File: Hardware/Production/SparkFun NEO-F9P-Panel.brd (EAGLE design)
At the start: 160.8 x 107.4 mm, 822 parts, among them J1 ANTENNA-SMA-GROUNDEDEDGE_SMA, J11 ANTENNA-SMA-GROUNDEDEDGE_SMA, J15 Qwiic Right Angle, J16 Qwiic Right Angle, J18 ANTENNA-SMA-GROUNDEDEDGE_SMA, J2 Qwiic Right Angle, J22 Qwiic Right Angle, J23 Qwiic Right Angle, J25 ANTENNA-SMA-GROUNDEDEDGE_SMA, J29 Qwiic Right Angle, J30 Qwiic Right Angle, J32 ANTENNA-SMA-GROUNDEDEDGE_SMA, J36 Qwiic Right Angle, J37 Qwiic Right Angle, J39 ANTENNA-SMA-GROUNDEDEDGE_SMA, J4 Qwiic Right Angle, J8 Qwiic Right Angle, J9 Qwiic Right Angle, U1 U-BLOX_NEO-F9P-15B, U10 U-BLOX_NEO-F9P-15B, U11 3.3V, U12 U-BLOX_NEO-F9P-15B, U2 3.3V, U3 3.3V, U4 U-BLOX_NEO-F9P-15B, U5 3.3V, U6 U-BLOX_NEO-F9P-15B, U7 3.3V, U8 U-BLOX_NEO-F9P-15B, U9 3.3V

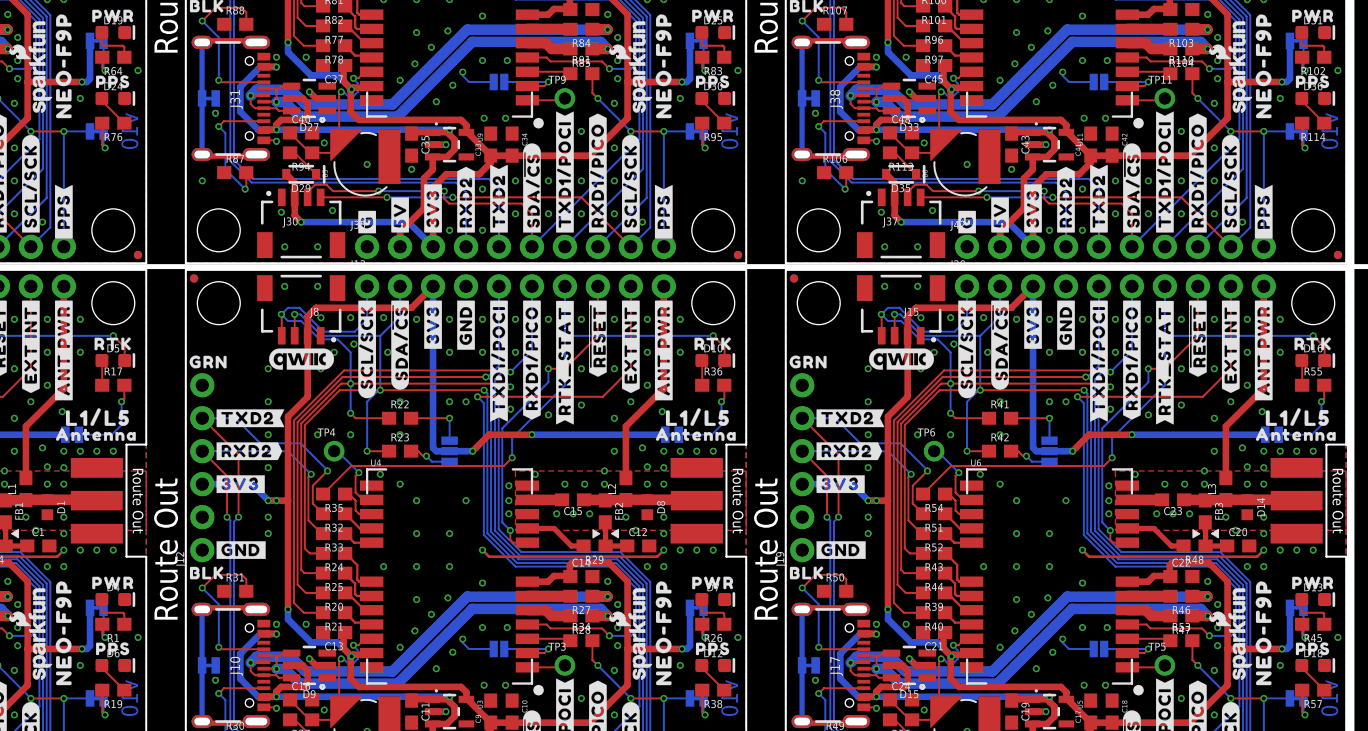
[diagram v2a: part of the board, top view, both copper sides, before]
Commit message: Adjust layout post design review.
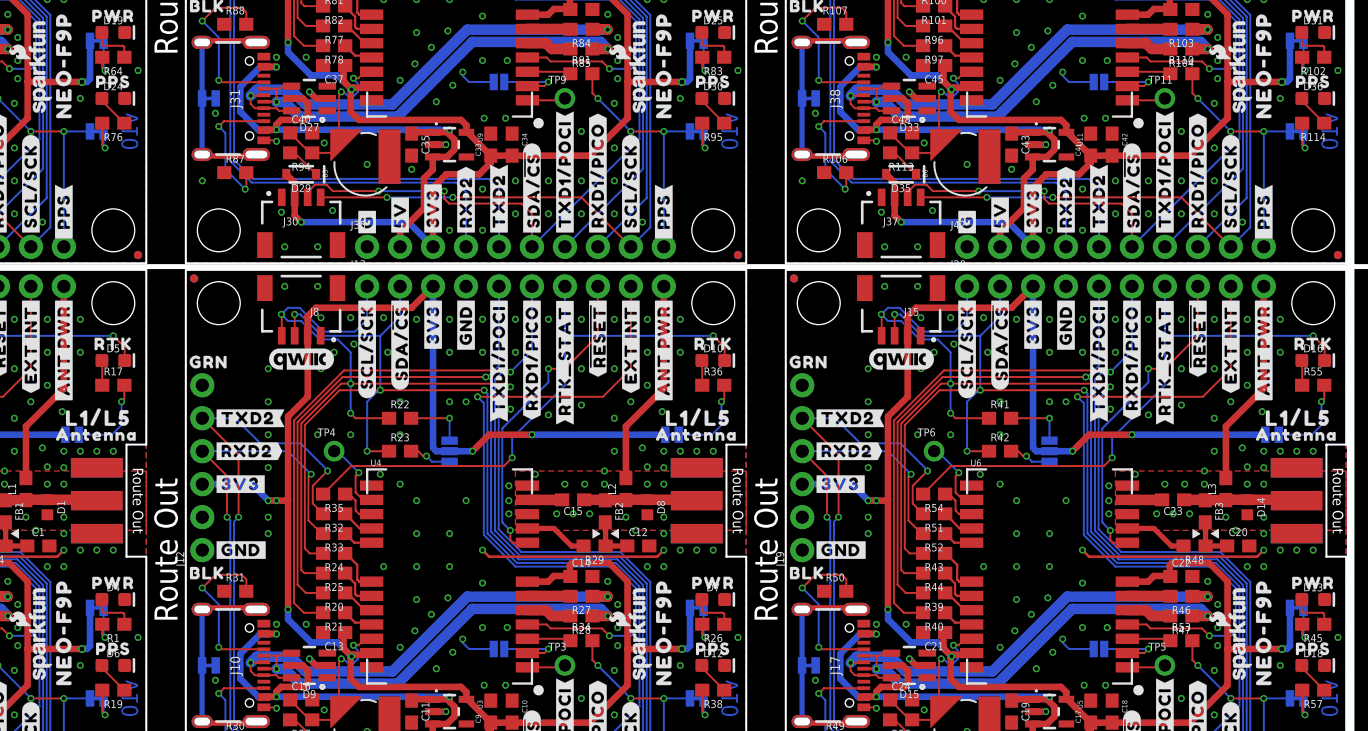
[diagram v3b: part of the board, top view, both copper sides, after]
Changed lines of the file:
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@@
 <wire x1="9.39" y1="38.1" x2="9.39" y2="33.3951875" width="0.508" layer="1"/>
 <wire x1="38.8493" y1="17.145" x2="38.8493" y2="14.2113" width="0.508" layer="16"/>
-<wire x1="38.8493" y1="14.2113" x2="38.608" y2="13.97" width="0.508" layer="16"/>
-<wire x1="38.608" y1="13.97" x2="38.227" y2="13.97" width="0.508" layer="16"/>
-<via x="38.227" y="13.97" extent="1-16" drill="0.3048"/>
 <wire x1="38.226996875" y1="13.97" x2="34.036" y2="13.97" width="0.508" layer="1"/>
 <contactref element="J6" pad="3"/>
@@
 <wire x1="22.098" y1="29.21" x2="20.32" y2="29.21" width="0.508" layer="16"/>
 <wire x1="36.9443" y1="30.48" x2="26.67" y2="30.48" width="0.508" layer="16"/>
-<wire x1="38.226996875" y1="13.97" x2="38.227" y2="13.97" width="0" layer="19" extent="1-1"/>
+<wire x1="38.8493" y1="14.2113" x2="38.608" y2="13.97" width="0.508" layer="16"/>
+<wire x1="38.608" y1="13.97" x2="38.226996875" y2="13.97" width="0.508" layer="16"/>
+<via x="38.226996875" y="13.97" extent="1-16" drill="0.381"/>
 </signal>
 <signal name="GND">
@@
 <wire x1="55.618" y1="38.1" x2="55.618" y2="33.3951875" width="0.508" layer="1"/>
 <wire x1="85.0773" y1="17.145" x2="85.0773" y2="14.2113" width="0.508" layer="16"/>
-<wire x1="85.0773" y1="14.2113" x2="84.836" y2="13.97" width="0.508" layer="16"/>
-<wire x1="84.836" y1="13.97" x2="84.455" y2="13.97" width="0.508" layer="16"/>
-<via x="84.455" y="13.97" extent="1-16" drill="0.3048"/>
 <wire x1="84.454996875" y1="13.97" x2="80.264" y2="13.97" width="0.508" layer="1"/>
 <contactref element="J14" pad="3"/>
@@
 <wire x1="68.326" y1="29.21" x2="66.548" y2="29.21" width="0.508" layer="16"/>
 <wire x1="83.1723" y1="30.48" x2="72.898" y2="30.48" width="0.508" layer="16"/>
-<wire x1="84.454996875" y1="13.97" x2="84.455" y2="13.97" width="0" layer="19" extent="1-1"/>
+<wire x1="85.0773" y1="14.2113" x2="84.836" y2="13.97" width="0.508" layer="16"/>
+<wire x1="84.836" y1="13.97" x2="84.454996875" y2="13.97" width="0.508" layer="16"/>
+<via x="84.454996875" y="13.97" extent="1-16" drill="0.381"/>
 </signal>
 <signal name="GND1">
@@
 <wire x1="101.846" y1="38.1" x2="101.846" y2="33.3951875" width="0.508" layer="1"/>
 <wire x1="131.3053" y1="17.145" x2="131.3053" y2="14.2113" width="0.508" layer="16"/>
-<wire x1="131.3053" y1="14.2113" x2="131.064" y2="13.97" width="0.508" layer="16"/>
-<wire x1="131.064" y1="13.97" x2="130.683" y2="13.97" width="0.508" layer="16"/>
-<via x="130.683" y="13.97" extent="1-16" drill="0.3048"/>
 <wire x1="130.682996875" y1="13.97" x2="126.492" y2="13.97" width="0.508" layer="1"/>
 <contactref element="J21" pad="3"/>
@@
 <wire x1="114.554" y1="29.21" x2="112.776" y2="29.21" width="0.508" layer="16"/>
 <wire x1="129.4003" y1="30.48" x2="119.126" y2="30.48" width="0.508" layer="16"/>
-<wire x1="130.682996875" y1="13.97" x2="130.683" y2="13.97" width="0" layer="19" extent="1-1"/>
+<wire x1="131.3053" y1="14.2113" x2="131.064" y2="13.97" width="0.508" layer="16"/>
+<wire x1="131.064" y1="13.97" x2="130.682996875" y2="13.97" width="0.508" layer="16"/>
+<via x="130.682996875" y="13.97" extent="1-16" drill="0.381"/>
 </signal>
 <signal name="GND2">
@@
 <wire x1="9.39" y1="81.788" x2="9.39" y2="77.0831875" width="0.508" layer="1"/>
 <wire x1="38.8493" y1="60.833" x2="38.8493" y2="57.8993" width="0.508" layer="16"/>
-<wire x1="38.8493" y1="57.8993" x2="38.608" y2="57.658" width="0.508" layer="16"/>
-<wire x1="38.608" y1="57.658" x2="38.227" y2="57.658" width="0.508" layer="16"/>
-<via x="38.227" y="57.658" extent="1-16" drill="0.3048"/>
 <wire x1="38.226996875" y1="57.658" x2="34.036" y2="57.658" width="0.508" layer="1"/>
 <contactref element="J28" pad="3"/>
@@
 <wire x1="22.098" y1="72.898" x2="20.32" y2="72.898" width="0.508" layer="16"/>
 <wire x1="36.9443" y1="74.168" x2="26.67" y2="74.168" width="0.508" layer="16"/>
-<wire x1="38.226996875" y1="57.658" x2="38.227" y2="57.658" width="0" layer="19" extent="1-1"/>
+<wire x1="38.8493" y1="57.8993" x2="38.608" y2="57.658" width="0.508" layer="16"/>
+<wire x1="38.608" y1="57.658" x2="38.226996875" y2="57.658" width="0.508" layer="16"/>
+<via x="38.226996875" y="57.658" extent="1-16" drill="0.381"/>
 </signal>
 <signal name="GND3">
@@
 <wire x1="55.618" y1="81.788" x2="55.618" y2="77.0831875" width="0.508" layer="1"/>
 <wire x1="85.0773" y1="60.833" x2="85.0773" y2="57.8993" width="0.508" layer="16"/>
-<wire x1="85.0773" y1="57.8993" x2="84.836" y2="57.658" width="0.508" layer="16"/>
-<wire x1="84.836" y1="57.658" x2="84.455" y2="57.658" width="0.508" layer="16"/>
-<via x="84.455" y="57.658" extent="1-16" drill="0.3048"/>
 <wire x1="84.454996875" y1="57.658" x2="80.264" y2="57.658" width="0.508" layer="1"/>
 <contactref element="J35" pad="3"/>
@@
 <wire x1="68.326" y1="72.898" x2="66.548" y2="72.898" width="0.508" layer="16"/>
 <wire x1="83.1723" y1="74.168" x2="72.898" y2="74.168" width="0.508" layer="16"/>
-<wire x1="84.454996875" y1="57.658" x2="84.455" y2="57.658" width="0" layer="19" extent="1-1"/>
+<wire x1="85.0773" y1="57.8993" x2="84.836" y2="57.658" width="0.508" layer="16"/>
+<wire x1="84.836" y1="57.658" x2="84.454996875" y2="57.658" width="0.508" layer="16"/>
+<via x="84.454996875" y="57.658" extent="1-16" drill="0.381"/>
 </signal>
 <signal name="GND4">
@@
 <wire x1="101.846" y1="81.788" x2="101.846" y2="77.0831875" width="0.508" layer="1"/>
 <wire x1="131.3053" y1="60.833" x2="131.3053" y2="57.8993" width="0.508" layer="16"/>
-<wire x1="131.3053" y1="57.8993" x2="131.064" y2="57.658" width="0.508" layer="16"/>
-<wire x1="131.064" y1="57.658" x2="130.683" y2="57.658" width="0.508" layer="16"/>
-<via x="130.683" y="57.658" extent="1-16" drill="0.3048"/>
 <wire x1="130.682996875" y1="57.658" x2="126.492" y2="57.658" width="0.508" layer="1"/>
 <contactref element="J42" pad="3"/>
@@
 <wire x1="114.554" y1="72.898" x2="112.776" y2="72.898" width="0.508" layer="16"/>
 <wire x1="129.4003" y1="74.168" x2="119.126" y2="74.168" width="0.508" layer="16"/>
-<wire x1="130.682996875" y1="57.658" x2="130.683" y2="57.658" width="0" layer="19" extent="1-1"/>
+<wire x1="131.3053" y1="57.8993" x2="131.064" y2="57.658" width="0.508" layer="16"/>
+<wire x1="131.064" y1="57.658" x2="130.682996875" y2="57.658" width="0.508" layer="16"/>
+<via x="130.682996875" y="57.658" extent="1-16" drill="0.381"/>
 </signal>
 <signal name="GND5">

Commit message: Increase version to v11
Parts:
- C1, C10, C12, C15, C18, C20, C23, C26, C28, C31, C34, C36, C39, C42, C44, C47, C5, C7: device SparkFun-Capacitors:0603@1 -> SparkFun-Capacitors:0603
- R10, R100, R101, R103, R104, R105, R106, R107, R108, R109, R11, R110, R111, R112, R114, R12, R13, R14, R15, R16, R17, R19, R2, R20, R21, R22, R23, R24, R25, R27, R28, R29, R3, R30, R31, R32, R33, R34, R35, R36, R38, R39, R4, R40, R41, R42, R43, R44, R46, R47, R48, R49, R5, R50, R51, R52, R53, R54, R55, R57, R58, R59, R6, R60, R61, R62, R63, R65, R66, R67, R68, R69, R7, R70, R71, R72, R73, R74, R76, R77, R78, R79, R8, R80, R81, R82, R84, R85, R86, R87, R88, R89, R9, R90, R91, R92, R93, R95, R96, R97, R98, R99: device SparkFun-Resistors:0603@1 -> SparkFun-Resistors:0603
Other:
- board text added: "v11"
- board text removed: "v10"
